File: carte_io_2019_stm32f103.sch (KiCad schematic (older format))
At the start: 25 parts, among them J1 Connecteur gauche, J10 capteur_couleur_S, J11 Tirette, J3 Alim logique, J4 Connecteur droit, J8 Liaison serie, J9 capteur_couleur_alim, Q1 PMF370XN, Q3 PMF370XN, Q4 PMF370XN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

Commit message: Ajout des capteurs de fin de course
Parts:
- removed R7: 10k, Resistor_SMD:R_1206_3216Metric_Pad1.42x1.75mm_HandSolder, symbol Device:R
- added J12: Buzzer, @Robot:HE14-3-straight, symbol Connector_Generic:Conn_01x03
- added J13: FinCourse1, TerminalBlock_Phoenix:TerminalBlock_Phoenix_MPT-0,5-2-2.54_1x02_P2.54mm_Horizontal, symbol Connector_Generic:Conn_01x02
- added J14: FinCourse2, TerminalBlock_Phoenix:TerminalBlock_Phoenix_MPT-0,5-2-2.54_1x02_P2.54mm_Horizontal, symbol Connector_Generic:Conn_01x02
- added J15: FinCourse3, TerminalBlock_Phoenix:TerminalBlock_Phoenix_MPT-0,5-2-2.54_1x02_P2.54mm_Horizontal, symbol Connector_Generic:Conn_01x02
- added J16: FinCourse4, TerminalBlock_Phoenix:TerminalBlock_Phoenix_MPT-0,5-2-2.54_1x02_P2.54mm_Horizontal, symbol Connector_Generic:Conn_01x02
- added J17: FinCourse5, TerminalBlock_Phoenix:TerminalBlock_Phoenix_MPT-0,5-2-2.54_1x02_P2.54mm_Horizontal, symbol Connector_Generic:Conn_01x02
- added J18: FinCourse6, TerminalBlock_Phoenix:TerminalBlock_Phoenix_MPT-0,5-2-2.54_1x02_P2.54mm_Horizontal, symbol Connector_Generic:Conn_01x02
- added J19: FinCourse7, TerminalBlock_Phoenix:TerminalBlock_Phoenix_MPT-0,5-2-2.54_1x02_P2.54mm_Horizontal, symbol Connector_Generic:Conn_01x02
- added J20: FinCourse8, TerminalBlock_Phoenix:TerminalBlock_Phoenix_MPT-0,5-2-2.54_1x02_P2.54mm_Horizontal, symbol Connector_Generic:Conn_01x02
- added J21: Piston, TerminalBlock_Phoenix:TerminalBlock_Phoenix_MPT-0,5-3-2.54_1x03_P2.54mm_Horizontal, symbol Connector_Generic:Conn_01x03
- J10, J9: footprint @Robot:HE14-4-straight -> TerminalBlock_Phoenix:TerminalBlock_Phoenix_MPT-0,5-4-2.54_1x04_P2.54mm_Horizontal
- J11: footprint @Robot:HE14-3-straight -> TerminalBlock_Phoenix:TerminalBlock_Phoenix_MPT-0,5-2-2.54_1x02_P2.54mm_Horizontal; symbol Connector_Generic:Conn_01x03 -> Connector_Generic:Conn_01x02
- J3, J8: footprint @Robot:HE14-3-straight -> TerminalBlock_Phoenix:TerminalBlock_Phoenix_MPT-0,5-3-2.54_1x03_P2.54mm_Horizontal
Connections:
- net labels added: buzzer, fin_course_1, fin_course_2, fin_course_3, fin_course_4, fin_course_5, fin_course_6, fin_course_7, fin_course_8, piston
- wire segments 36 -> 62
- no-connect marks 27 -> 18
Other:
- moved on the sheet: J10, J9, TP1

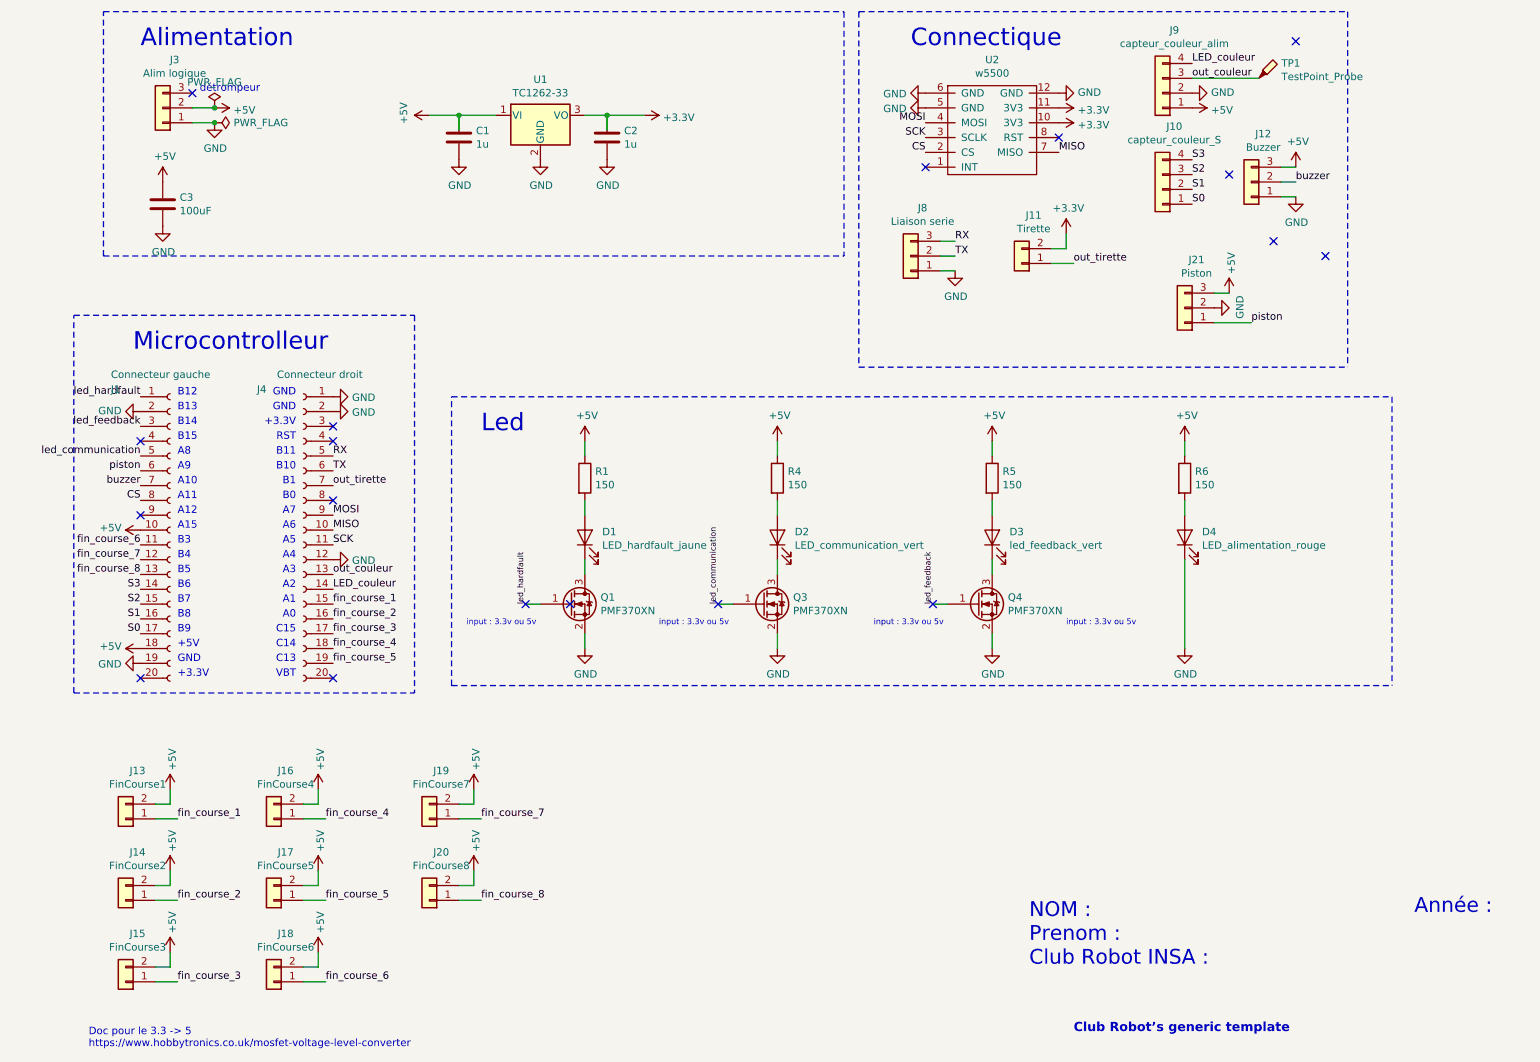
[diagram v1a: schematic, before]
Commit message: Fix buzzer
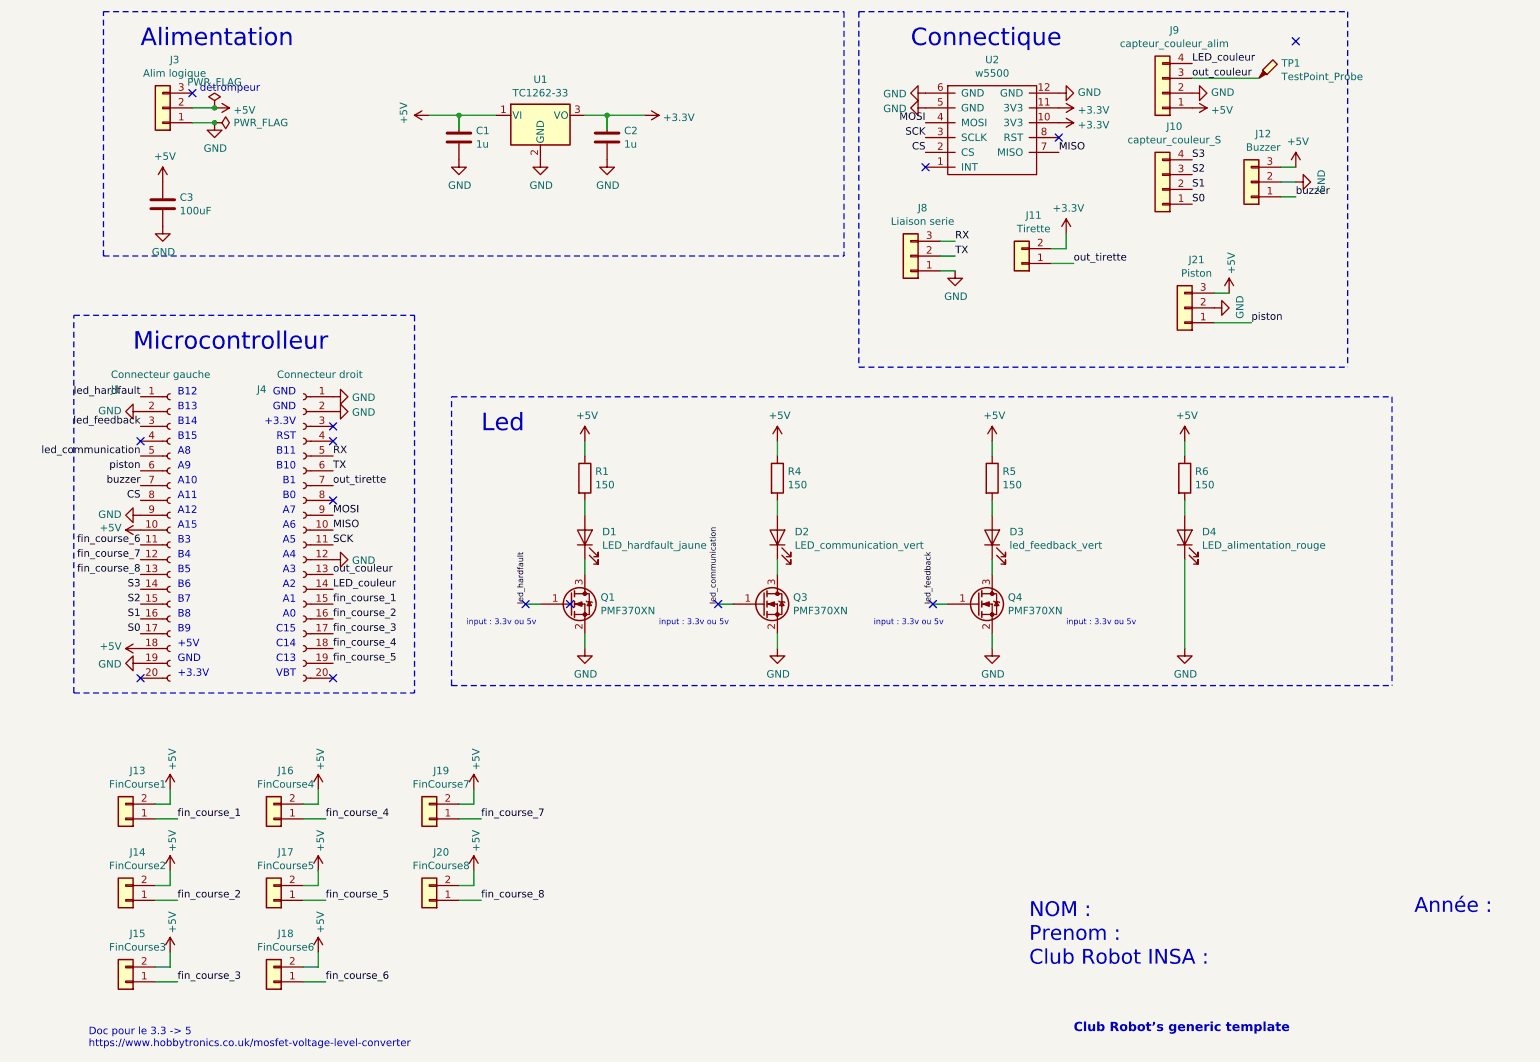
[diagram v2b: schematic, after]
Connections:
- net GND: now also J1.9 (Pin_9), J12.2 (Pin_2); no longer J12.1 (Pin_1)
- net buzzer: now also J12.1 (Pin_1); no longer J12.2 (Pin_2)
- no-connect marks 18 -> 14
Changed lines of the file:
@@
 L power:GND #PWR0125
 U 1 1 5CD45D50
-P 8850 1850
-F 0 "#PWR0125" H 8850 1600 50  0001 C CNN
-F 1 "GND" H 8855 1677 50  0000 C CNN
-F 2 "" H 8850 1850 50  0001 C CNN
-F 3 "" H 8850 1850 50  0001 C CNN
-	1    8850 1850
-	1    0    0    -1
+P 8850 1750
+F 0 "#PWR0125" H 8850 1500 50  0001 C CNN
+F 1 "GND" H 8855 1577 50  0000 C CNN
+F 2 "" H 8850 1750 50  0001 C CNN
+F 3 "" H 8850 1750 50  0001 C CNN
+	1    8850 1750
+	0    -1   -1   0
 $EndComp
 $Comp
@@
 	1    0    0    -1
 $EndComp
-Text Label 8850 1750 0    50   ~ 0
+Text Label 8850 1850 0    50   ~ 0
 buzzer
 Text Label 1050 3800 2    50   ~ 0
@@
 	1    0    0    -1
 $EndComp
-NoConn ~ 1050 4000
-NoConn ~ 8400 1700
-NoConn ~ 9050 2250
-NoConn ~ 8700 2150
 Text Label 1050 3700 2    50   ~ 0
 piston
@@
 NoConn ~ 8850 800
 $Comp
-L power:GND #PWR?
+L power:GND #PWR0145
 U 1 1 5CE263A9
 P 1050 3300
-F 0 "#PWR?" H 1050 3050 50  0001 C CNN
+F 0 "#PWR0145" H 1050 3050 50  0001 C CNN
 F 1 "GND" V 1055 3172 50  0000 R CNN
 F 2 "" H 1050 3300 50  0001 C CNN
@@
 	0    1    -1   0
 $EndComp
+$Comp
+L power:GND #PWR?
+U 1 1 5CDECC4E
+P 1050 4000
+F 0 "#PWR?" H 1050 3750 50  0001 C CNN
+F 1 "GND" V 1055 3872 50  0000 R CNN
+F 2 "" H 1050 4000 50  0001 C CNN
+F 3 "" H 1050 4000 50  0001 C CNN
+	1    1050 4000
+	0    1    -1   0
+$EndComp

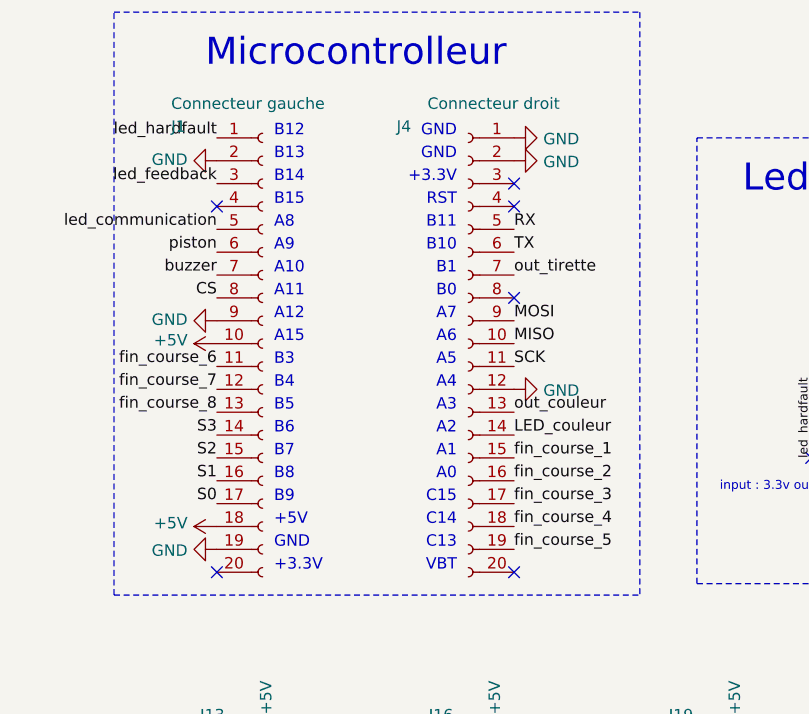
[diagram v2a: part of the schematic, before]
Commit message: Replacage de led_feedback sur PC13
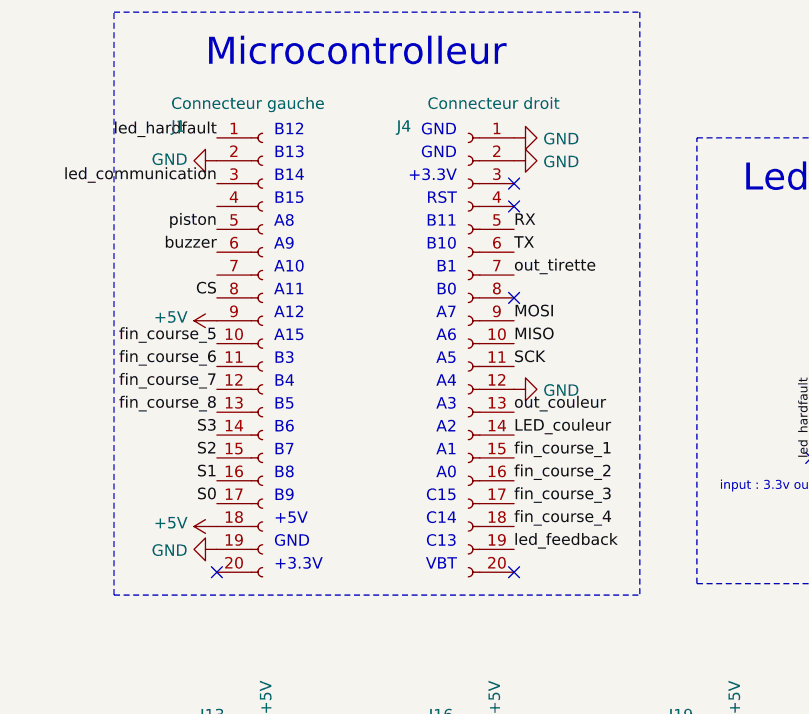
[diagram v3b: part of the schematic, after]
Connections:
- net +5V: now also J1.9 (Pin_9); no longer J1.10 (Pin_10)
- net GND: no longer J1.9 (Pin_9)
- net buzzer: now also J1.6 (Pin_6); no longer J1.7 (Pin_7)
- net fin_course_5: now also J1.10 (Pin_10); no longer J4.19 (Pin_19)
- net led_communication: now also J1.3 (Pin_3); no longer J1.5 (Pin_5)
- net led_feedback: now also J4.19 (Pin_19); no longer J1.3 (Pin_3)
- net piston: now also J1.5 (Pin_5); no longer J1.6 (Pin_6)
- no-connect marks 14 -> 13
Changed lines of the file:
@@
 NoConn ~ 2350 5100
 NoConn ~ 2350 3500
-NoConn ~ 1050 3500
 $Comp
 L Device:Q_NMOS_GSD Q1
@@
 Text Label 1050 3200 2    50   ~ 0
 led_hardfault
+Text Label 2350 5000 0    50   ~ 0
+led_feedback
 Text Label 1050 3400 2    50   ~ 0
-led_feedback
-Text Label 1050 3600 2    50   ~ 0
 led_communication
 Wire Wire Line
@@
 L power:+5V #PWR0133
 U 1 1 5CCB0A44
-P 1050 4100
-F 0 "#PWR0133" H 1050 3950 50  0001 C CNN
-F 1 "+5V" V 1065 4228 50  0000 L CNN
-F 2 "" H 1050 4100 50  0001 C CNN
-F 3 "" H 1050 4100 50  0001 C CNN
-	1    1050 4100
+P 1050 4000
+F 0 "#PWR0133" H 1050 3850 50  0001 C CNN
+F 1 "+5V" V 1065 4128 50  0000 L CNN
+F 2 "" H 1050 4000 50  0001 C CNN
+F 3 "" H 1050 4000 50  0001 C CNN
+	1    1050 4000
 	0    -1   -1   0
 $EndComp
@@
 Text Label 8850 1850 0    50   ~ 0
 buzzer
-Text Label 1050 3800 2    50   ~ 0
+Text Label 1050 3700 2    50   ~ 0
 buzzer
 Wire Wire Line
@@
 Text Label 1050 4200 2    50   ~ 0
 fin_course_6
-Text Label 2350 5000 0    50   ~ 0
+Text Label 1050 4100 2    50   ~ 0
 fin_course_5
 Text Label 1050 4300 2    50   ~ 0
@@
 	1    0    0    -1
 $EndComp
-Text Label 1050 3700 2    50   ~ 0
+Text Label 1050 3600 2    50   ~ 0
 piston
 Wire Wire Line
@@
 	0    1    -1   0
 $EndComp
-$Comp
-L power:GND #PWR?
-U 1 1 5CDECC4E
-P 1050 4000
-F 0 "#PWR?" H 1050 3750 50  0001 C CNN
-F 1 "GND" V 1055 3872 50  0000 R CNN
-F 2 "" H 1050 4000 50  0001 C CNN
-F 3 "" H 1050 4000 50  0001 C CNN
-	1    1050 4000
-	0    1    -1   0
-$EndComp

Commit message: Add metadata to schematic and PCB
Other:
- note removed: "Club Robot’s generic template"
- note removed: "NOM : \nPrenom : \nClub Robot INSA :"
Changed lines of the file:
@@
 EESchema Schematic File Version 4
 LIBS:carte_io_2019_stm32f103-cache
-EELAYER 26 0
+EELAYER 29 0
 EELAYER END
 $Descr A4 11693 8268
 encoding utf-8
 Sheet 1 1
-Title ""
-Date ""
-Rev ""
-Comp ""
-Comment1 ""
-Comment2 ""
+Title "Carte IO Petit robot"
+Date "2019-05-17"
+Rev "v1"
+Comp "Club Robot"
+Comment1 "Paul"
+Comment2 "Meis"
 Comment3 ""
 Comment4 ""
@@
 Wire Notes Line
 	600  5200 2900 5200
-Text Notes 7050 7050 0    100  ~ 0
-NOM : \nPrenom : \nClub Robot INSA :
 Text Notes 9650 6700 0    100  ~ 0
 Année :
-Text Notes 7350 7500 0    62   ~ 12
-Club Robot’s generic template
 NoConn ~ 1050 5100
 NoConn ~ 2350 3400
